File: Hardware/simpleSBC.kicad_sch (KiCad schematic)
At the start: 124 parts, among them J1 Conn_02x07_Odd_Even, J2 Micro_SD_Card_Det, J3 Conn_01x06_Male, U1 STM32MP157FAD1, U2 LP2998, U3 MT41K256M16TW, X1 ASCO, Y1 32.786

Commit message: Add STPMIC1
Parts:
- added C67, C68, C69, C70: 10u, Capacitor_SMD:C_0402_1005Metric, symbol Device:C_Small
- added C71, C72, C73, C74, C75: 1u, Capacitor_SMD:C_0402_1005Metric, symbol Device:C_Small
- added C76: 4.7u, Capacitor_SMD:C_0402_1005Metric, symbol Device:C_Small
- added L1, L2, L3, L4: L_Small, symbol Device:L_Small
- added R9: R_Small, symbol Device:R_Small
- added TP10: TestPoint, symbol Connector:TestPoint
- added U4: STPMIC1, BioMEMS:WFQFN44L, symbol BioMEMS:STPMIC1APQR
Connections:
- net +1V2: now also L1.2, U4.5 (VOUT1)
- net +1V35: now also L2.2, U4.13 (LDO3IN), U4.9 (VOUT2)
- net +3V3: now also L4.2, U4.31 (VOUT3), U4.42 (VIO)
- net GND: now also C67.1, C68.1, C69.1, C70.1, C71.2, C72.2, C73.2, C74.1, C75.1, C76.1, U4.10 (PGND2), U4.15 (GNDLDO), U4.26 (PGND4), U4.30 (PGND3), U4.32 (PGND5), U4.41 (AGND), U4.45 (EPGND), U4.6 (PGND1)
- net NRST: now also U4.1 (RSTn)
- net PWR_ON: now also U4.44 (PWRCTRL)
- net VREF_DDR: now also C74.2, U4.16 (VREFDDR)
- net VTT_DDR: now also C75.2, U4.14 (LDO3OUT)
- net PA0_WAKEUP: now reaches U1.N3 (PA0)
- net PA0_WAKEUP: now also U4.43 (INTn)
- new net: L1.1, U4.7 (VLX1)
- new net: R9.2, U4.37 (SWIN)
- new net: L2.1, U4.11 (VLX2)
- new net: TP10.1, U4.17 (PONKEYn)
- new net: L3.1, U4.25 (VLX4)
- new net: L4.1, U4.29 (VLX3)
- new net: C76.2, U4.40 (INTLDO)
- new net +3.3VP: C72.1, L3.2, U4.22 (LDO16IN), U4.27 (VOUT4)
- new net +5V: C67.2, C68.2, C69.2, C70.2, C71.1, C73.1, R9.1, U4.12 (BUCK2IN), U4.19 (LDO25IN), U4.24 (BUCK4IN), U4.28 (BUCK3IN), U4.33 (VLXBST), U4.36 (VIN), U4.8 (BUCK1IN)
- new net I2C4_SCL: U4.4 (SCL)
- new net I2C4_SDA: U4.3 (SDA)
- new net PMIC_WAKEUP: U4.2 (WAKEUP)
- no-connect marks 101 -> 108
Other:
- moved on the sheet: C1, C10, C11, C12, C13, C14, C15, C16, C17, C18, C19, C2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

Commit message: Remove old files
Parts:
- removed C1, C11, C13, C15, C18, C21, C23, C24, C26, C28, C3, C30, C31, C32, C35, C38, C42, C45, C48, C5, C7, C71, C72, C73, C74, C75: 1u, Capacitor_SMD:C_0402_1005Metric, symbol Device:C_Small
- removed C10, C17: 1n, Capacitor_SMD:C_0402_1005Metric, symbol Device:C_Small
- removed C12, C14, C16, C19, C2, C20, C22, C25, C27, C4, C46, C47, C49, C50, C52, C53, C54, C55, C56, C57, C58, C59, C6, C60, C61, C62, C63, C64, C8, C9: 100n, Capacitor_SMD:C_0402_1005Metric, symbol Device:C_Small
- removed C33, C34: 10u, Capacitor_SMD:C_0805_2012Metric, symbol Device:C_Small
- removed C39, C43, C44: 100u, Capacitor_SMD:C_1206_3216Metric, symbol Device:C_Polarized_Small_US
- removed C41, C76: 4.7u, Capacitor_SMD:C_0402_1005Metric, symbol Device:C_Small
- removed C51: 4.7u, Capacitor_SMD:C_0603_1608Metric, symbol Device:C_Small
- removed C65, C66: 22u, Capacitor_SMD:C_0805_2012Metric, symbol Device:C_Small
- removed C67, C68, C69, C70: 10u, Capacitor_SMD:C_0402_1005Metric, symbol Device:C_Small
- removed J2: Micro_SD_Card_Det, Connector_Card:microSD_HC_Molex_104031-0811, symbol Connector:Micro_SD_Card_Det
- removed JP1: SolderJumper_2_Bridged, Jumper:SolderJumper-2_P1.3mm_Bridged2Bar_Pad1.0x1.5mm, symbol Jumper:SolderJumper_2_Bridged
- removed L1, L2, L3, L4: L_Small, symbol Device:L_Small
- removed R1, R4: 240, Resistor_SMD:R_0402_1005Metric, symbol Device:R_Small
- removed R10, R11, R12, R13, R14: 47k, Resistor_SMD:R_0402_1005Metric, symbol Device:R_Small
- removed R15, R3, R5: 10k, Resistor_SMD:R_0402_1005Metric, symbol Device:R_Small
- removed R16, R17, R18, R19, R20, R21, R22, R23, R24, R25, R26, R27, R28, R29, R30, R31, R32, R33, R34, R35, R36, R37, R38, R39: 56, Resistor_SMD:R_0402_1005Metric, symbol Device:R_Small
- removed R2: 100, Resistor_SMD:R_0402_1005Metric, symbol Device:R_Small
- removed R9: R_Small, symbol Device:R_Small
- removed TP1, TP2, TP3, TP4, TP5, TP6: TestPoint-SP, personal:PROBE_PAD_1206, symbol Connector:TestPoint
- removed TP10: TestPoint, symbol Connector:TestPoint
- removed TP7, TP9: TestPoint, personal:PROBE_PAD_1206, symbol Connector:TestPoint
- removed unit 4 of U1
- removed unit 1 of U1
- removed U2: LP2998, Package_SO:SOIC-8-1EP_3.9x4.9mm_P1.27mm_EP2.29x3mm_ThermalVias, symbol Personal:LP2998
- removed U3: MT41K256M16TW, Package_BGA:BGA-96_9.0x13.0mm_Layout2x3x16_P0.8mm, symbol Personal:MT41K256M16TW
- removed U4: STPMIC1, BioMEMS:WFQFN44L, symbol BioMEMS:STPMIC1APQR
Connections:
- no-connect marks 108 -> 92
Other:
- added sheet Memory (memory.kicad_sch)
- added sheet Power (power.kicad_sch)
- note removed: "100nF"
- note removed: "Connect VDDQ near memory"
- note removed: "RAM"
- note removed: "SD Card"
- note removed: "Termination"
- note removed: "VDD"
- note removed: "VDDCORE"
- note removed: "VDD_DSI, VDD_PLL and VDD_ANA must be star-connected to VDD"
- moved on the sheet: C29, C36, C37, C40, D1, J1, J3, R40, R6, R7, R8, TP8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

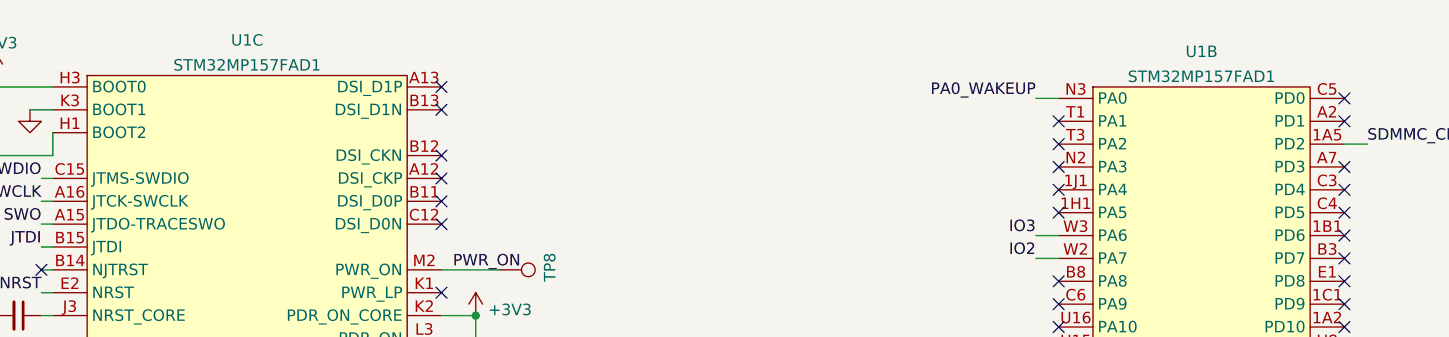
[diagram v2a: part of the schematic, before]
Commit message: Create libraries and move custom symbols to project specific libraries
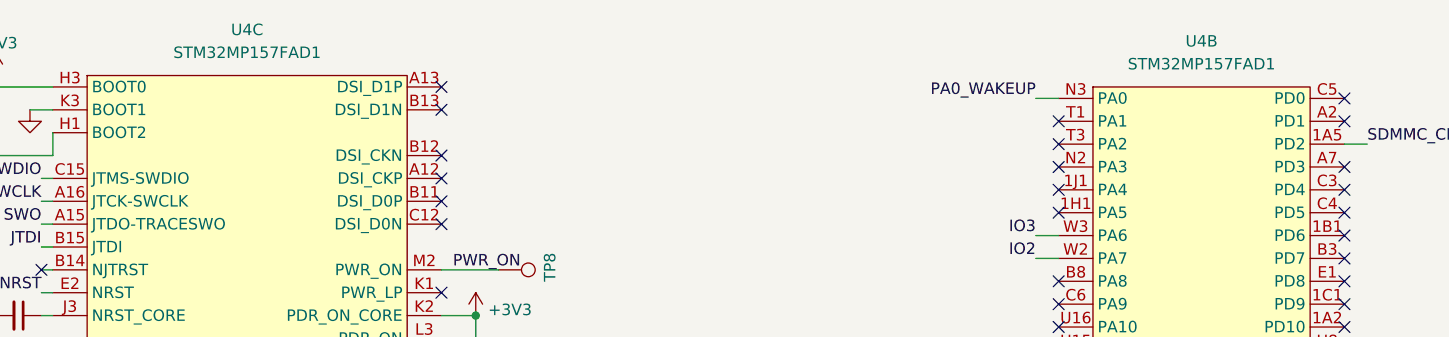
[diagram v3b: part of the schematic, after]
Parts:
- removed U1: STM32MP157FAD1, personal:TFBGA257, symbol Personal:STM32MP157FAD1
- added U4: STM32MP157FAD1, personal:TFBGA257, symbol SimpleSBC:STM32MP157FAD1
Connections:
- net +3V3: now also U4.H1 (BOOT2), U4.H3 (BOOT0), U4.K2 (PDR_ON_CORE), U4.L3 (PDR_ON)
- net GND: now also U4.A3 (PB7), U4.K3 (BOOT1)
- net IO1: now also U4.V1 (PC5)
- net IO2: now also U4.W2 (PA7)
- net IO3: now also U4.W3 (PA6)
- net IO4: now also U4.W4 (PF11)
- net IO5: now also U4.W7 (PF7)
- net IO6: now also U4.W8 (PG9)
- net JTDI: now also U4.B15 (JTDI)
- net NRST: now also U4.E2 (NRST)
- net PA0_WAKEUP: now also U4.N3 (PA0)
- net PWR_ON: now also U4.M2 (PWR_ON)
- net SDMMC_CLK: now also U4.1B4 (PC12)
- net SDMMC_CMD: now also U4.1A5 (PD2)
- net SDMMC_D0: now also U4.A9 (PC8)
- net SDMMC_D1: now also U4.B9 (PC9)
- net SDMMC_D2: now also U4.B10 (PC10)
- net SDMMC_D3: now also U4.C11 (PC11)
- net SWCLK: now also U4.A16 (JTCK-SWCLK)
- net SWDIO: now also U4.C15 (JTMS-SWDIO)
- net SWO: now also U4.A15 (JTDO-TRACESWO)
- net UART4_RX: now also U4.V13 (PB2)
- net UART4_TX: now also U4.U6 (PG11)
- net at C37.2, Y1.1: now also U4.F2 (PC15-OSC32_OUT)
- net at C36.2, Y1.2: now also U4.G2 (PC14-OSC32_IN)
- net at R40.2: now also U4.L2 (PA13)
- net at C40.1: now also U4.J3 (NRST_CORE)
- net at R8.2: now also U4.J2 (PH1-OSC_OUT)
- net at X1.3 (OUT): now also U4.H2 (PH0-OSC_IN)

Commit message: First Draft schematic (R2)
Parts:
- removed U4: STM32MP157FAD1, personal:TFBGA257, symbol SimpleSBC:STM32MP157FAD1
- added J5, J6: USB_A, Connector_USB:USB_A_Molex_67643_Horizontal, symbol Connector:USB_A
- added U1: STM32MP157FAD1, SimpleSBC:TFBGA257, symbol SimpleSBC:STM32MP157FAD1
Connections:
- net +3V3: now also U1.H1 (BOOT2), U1.H3 (BOOT0), U1.K2 (PDR_ON_CORE), U1.L3 (PDR_ON)
- net GND: now also J5.4 (GND), J5.5 (Shield), J6.4 (GND), J6.5 (Shield), U1.A3 (PB7), U1.K3 (BOOT1)
- net IO1: now also U1.V1 (PC5)
- net IO2: now also U1.W2 (PA7)
- net IO3: now also U1.W3 (PA6)
- net IO4: now also U1.W4 (PF11)
- net IO5: now also U1.W7 (PF7)
- net IO6: now also U1.W8 (PG9)
- net JTDI: now also U1.B15 (JTDI)
- net NRST: now also U1.E2 (NRST)
- net PA0_WAKEUP: now also U1.N3 (PA0)
- net PWR_ON: now also U1.M2 (PWR_ON)
- net SDMMC_CLK: now also U1.1B4 (PC12)
- net SDMMC_CMD: now also U1.1A5 (PD2)
- net SDMMC_D0: now also U1.A9 (PC8)
- net SDMMC_D1: now also U1.B9 (PC9)
- net SDMMC_D2: now also U1.B10 (PC10)
- net SDMMC_D3: now also U1.C11 (PC11)
- net SWCLK: now also U1.A16 (JTCK-SWCLK)
- net SWDIO: now also U1.C15 (JTMS-SWDIO)
- net SWO: now also U1.A15 (JTDO-TRACESWO)
- net UART4_RX: now also U1.V13 (PB2)
- net UART4_TX: now also U1.U6 (PG11)
- net at C37.2, Y1.1: now also U1.F2 (PC15-OSC32_OUT)
- net at C36.2, Y1.2: now also U1.G2 (PC14-OSC32_IN)
- net at R40.2: now also U1.L2 (PA13)
- net at X1.3 (OUT): now also U1.H2 (PH0-OSC_IN)
- net at R8.2: now also U1.J2 (PH1-OSC_OUT)
- net at C40.1: now also U1.J3 (NRST_CORE)
- new net: J5.2 (D-), U1.W10 (USB_DM2)
- new net: J5.3 (D+), U1.V10 (USB_DP2)
- new net: J6.2 (D-), U1.V14 (USB_DP1)
- new net: J6.3 (D+), U1.W14 (USB_DM1)
- no-connect marks 92 -> 90
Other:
- note added: "TODO: - I2C for STPMIC should be broken out - Add USB and Ethernet - USB Power?"
- title: Application Processor Test -> SimpleSBC
- moved on the sheet: J3

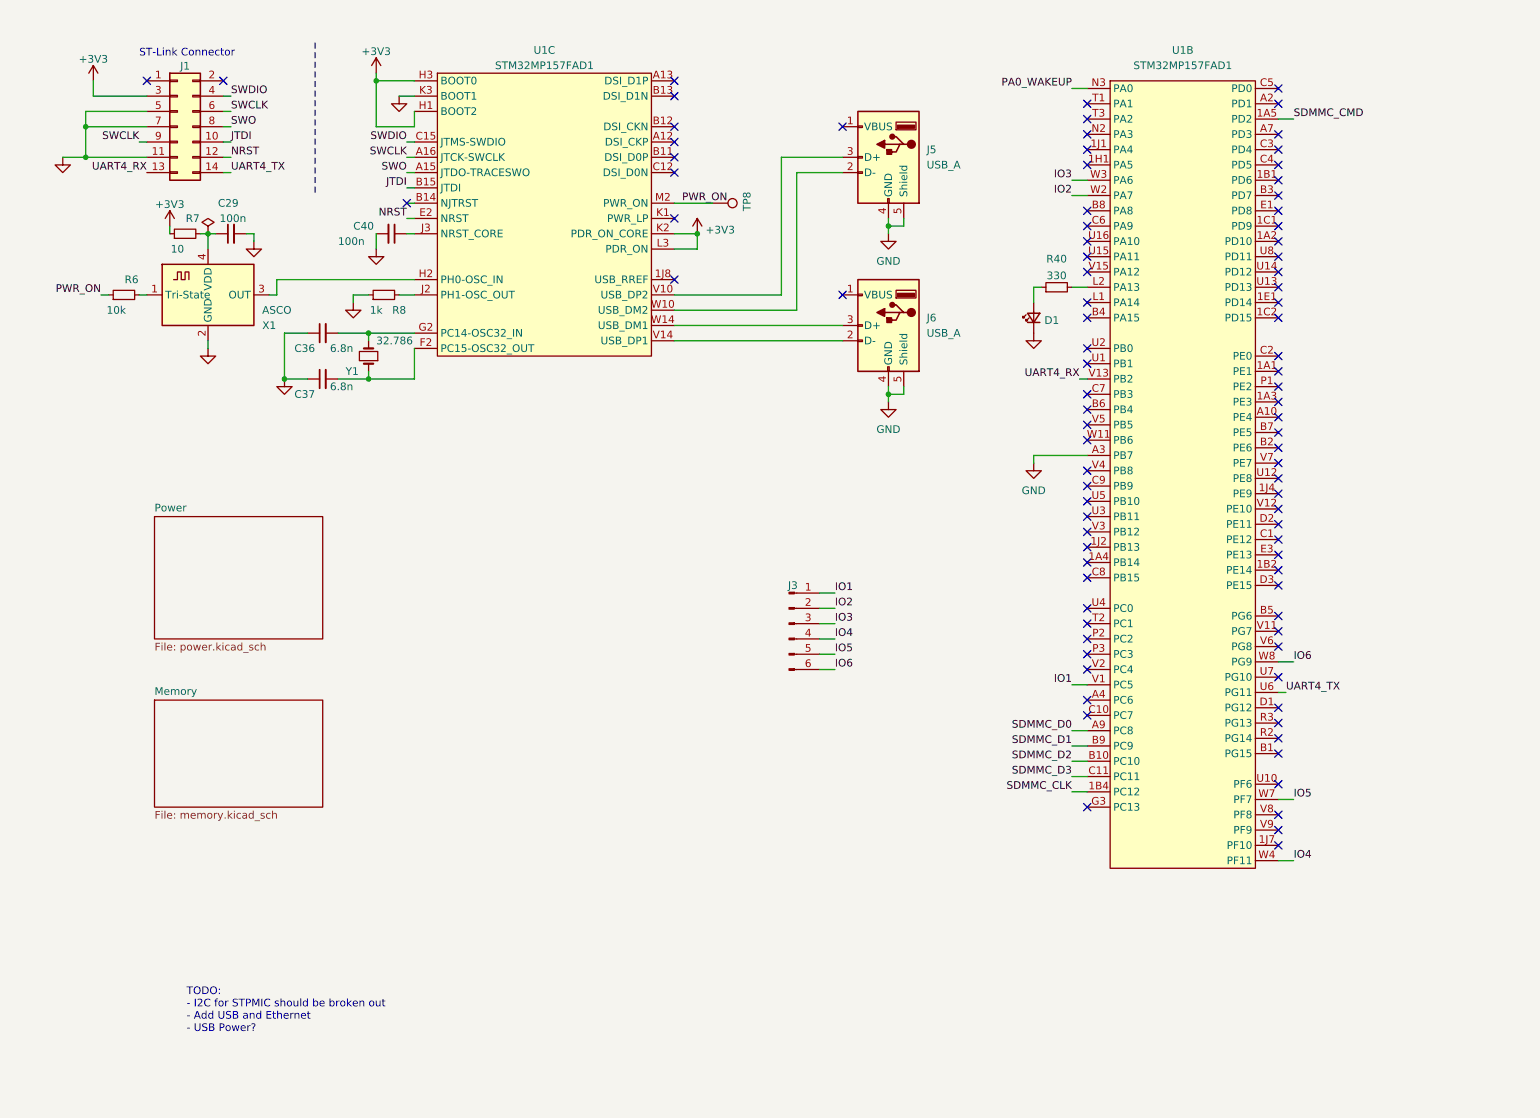
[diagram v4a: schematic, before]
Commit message: Add Ethernet and USB power switching
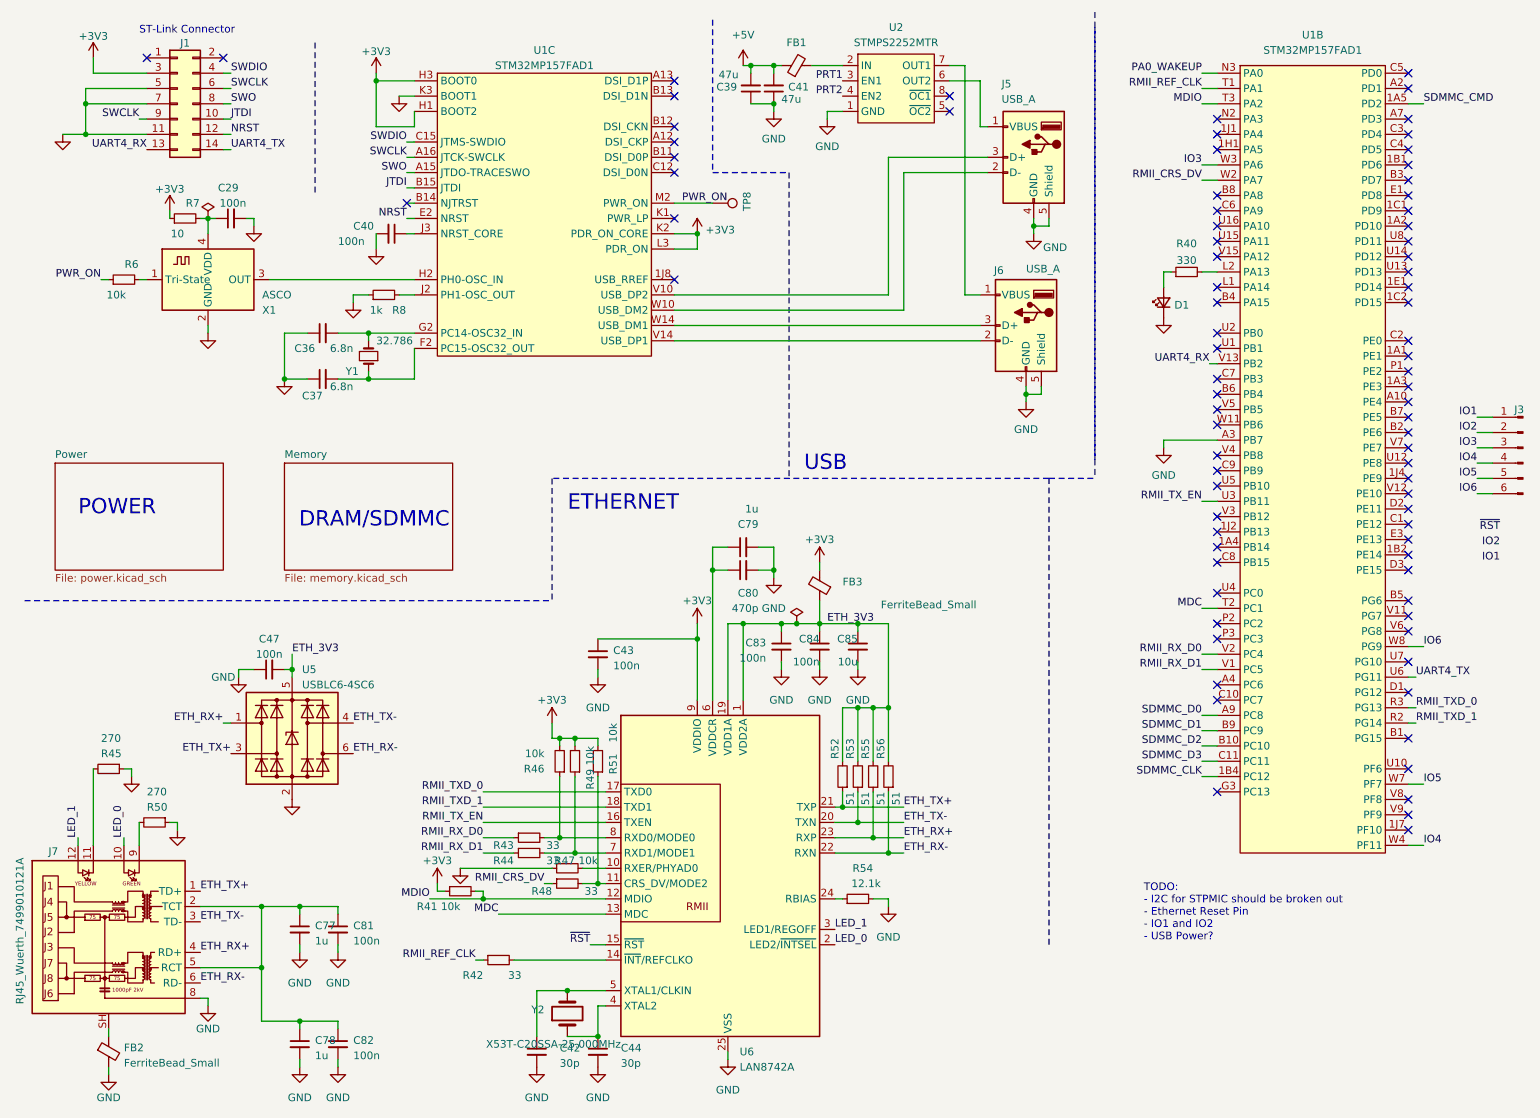
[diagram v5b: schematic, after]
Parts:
- added C39, C41: 47u, Capacitor_SMD:C_0402_1005Metric, symbol Device:C_Small
- added C42, C44: 30p, Capacitor_SMD:C_0603_1608Metric, symbol Device:C_Small
- added C43, C47, C81, C82, C83, C84: 100n, Capacitor_SMD:C_0603_1608Metric, symbol Device:C_Small
- added C77, C78, C79: 1u, Capacitor_SMD:C_0603_1608Metric, symbol Device:C_Small
- added C80: 470p, Capacitor_SMD:C_0603_1608Metric, symbol Device:C_Small
- added C85: 10u, Capacitor_SMD:C_0805_2012Metric, symbol Device:C_Small
- added FB1: FerriteBead_Small, symbol Device:FerriteBead_Small
- added FB2, FB3: FerriteBead_Small, Inductor_SMD:L_0603_1608Metric, symbol Device:FerriteBead_Small
- added J7: RJ45_Wuerth_7499010121A, Connector_RJ:RJ45_Wuerth_7499010121A_Horizontal, symbol SimpleSBC:RJ45_Wuerth_7499010121A
- added R41, R46, R47, R49, R51: 10k, Resistor_SMD:R_0603_1608Metric, symbol Device:R_Small
- added R42, R43, R44, R48: 33, Resistor_SMD:R_0603_1608Metric, symbol Device:R_Small
- added R45, R50: 270, Resistor_SMD:R_0603_1608Metric, symbol Device:R_Small
- added R52, R53, R55, R56: 51, Resistor_SMD:R_0603_1608Metric, symbol Device:R_Small
- added R54: 12.1k, Resistor_SMD:R_0603_1608Metric, symbol Device:R_Small
- added U2: STMPS2252MTR, Package_SO:SOIC-8_3.9x4.9mm_P1.27mm, symbol SimpleSBC:STMPS2252MTR
- added U5: USBLC6-4SC6, Package_TO_SOT_SMD:SOT-23-6, symbol Power_Protection:USBLC6-4SC6
- added U6: LAN8742A, Package_DFN_QFN:VQFN-24-1EP_4x4mm_P0.5mm_EP2.5x2.5mm_ThermalVias, symbol Interface_Ethernet:LAN8742A
- added Y2: X53T-C20SSA-25.000MHz, Crystal:Crystal_SMD_MicroCrystal_CM9V-T1A-2Pin_1.6x1.0mm, symbol Device:Crystal
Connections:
- net +3V3: now also C43.1, FB3.2, R41.1, R46.2, R49.2, R51.2, U6.9 (VDDIO)
- net GND: now also C39.1, C41.1, C42.2, C43.2, C44.2, C47.1, C77.2, C78.2, C79.2, C80.2, C81.2, C82.2, C83.2, C84.2, C85.2, FB2.2, J7.8, R45.1, R47.1, R50.1, R54.2, U2.1 (GND), U5.2 (GND), U6.25 (VSS)
- net IO1: no longer U1.V1 (PC5)
- net IO2: no longer U1.W2 (PA7)
- net at J5.1 (VBUS): now also U2.6 (OUT2)
- net at J6.1 (VBUS): now also U2.7 (OUT1)
- net RMII_TXD_1: now reaches U1.R2 (PG14)
- net RMII_TXD_1: now also U6.18 (TXD1)
- net RMII_TXD_0: now reaches U1.R3 (PG13)
- net RMII_TXD_0: now also U6.17 (TXD0)
- net RMII_REF_CLK: now reaches U1.T1 (PA1)
- net RMII_REF_CLK: now also R42.1
- net MDC: now reaches U1.T2 (PC1)
- net MDC: now also U6.13 (MDC)
- net MDIO: now reaches U1.T3 (PA2)
- net MDIO: now also R41.2, U6.12 (MDIO)
- net RMII_TX_EN: now reaches U1.U3 (PB11)
- net RMII_TX_EN: now also U6.16 (TXEN)
- net RMII_RX_D0: now reaches U1.V2 (PC4)
- net RMII_RX_D0: now also R43.1
- new net: R48.2, R51.1, U6.11 (CRS_DV/MODE2)
- new net: C77.1, C78.1, C81.1, C82.1, J7.2 (TCT), J7.5 (RCT)
- new net: C79.1, C80.1, U6.6 (VDDCR)
- new net: J7.9, R50.2
- new net: R44.2, R49.1, U6.7 (RXD1/MODE1)
- new net: J7.11, R45.2
- new net: FB2.1, J7.SH
- new net: R47.2, U6.10 (RXER/PHYAD0)
- new net: R42.2, U6.14 (~{INT}/REFCLKO)
- new net: R54.1, U6.24 (RBIAS)
- new net: C44.1, U6.4 (XTAL2), Y2.1
- new net: C42.1, U6.5 (XTAL1/CLKIN), Y2.2
- new net: R43.2, R46.1, U6.8 (RXD0/MODE0)
- new net: FB1.2, U2.2 (IN)
- new net +5V: C39.2, C41.2, FB1.1
- new net ETH_3V3: C47.2, C83.1, C84.1, C85.1, FB3.1, R52.2, R53.2, R55.2, R56.2, U5.5 (VBUS), U6.1 (VDD2A), U6.19 (VDD1A)
- new net ETH_RX+: J7.4 (RD+), R55.1, U5.1 (I/O1), U6.23 (RXP)
- new net ETH_RX-: J7.6 (RD-), R56.1, U5.6 (I/O4), U6.22 (RXN)
- new net ETH_TX+: J7.1 (TD+), R52.1, U5.3 (I/O2), U6.21 (TXP)
- new net ETH_TX-: J7.3 (TD-), R53.1, U5.4 (I/O3), U6.20 (TXN)
- new net LED_0: J7.10, U6.2 (LED2/~{INTSEL})
- new net LED_1: J7.12, U6.3 (LED1/REGOFF)
- new net PRT1: U2.3 (EN1)
- new net PRT2: U2.4 (EN2)
- new net RMII_CRS_DV: R48.1, U1.W2 (PA7)
- new net RMII_RX_D1: R44.1, U1.V1 (PC5)
- new net ~{RST}: U6.15 (~{RST})
- no-connect marks 90 -> 83
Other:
- note added: "DRAM/SDMMC"
- note added: "ETHERNET"
- note added: "POWER"
- note added: "TODO: - I2C for STPMIC should be broken out - Ethernet Reset Pin - IO1 and IO2 - USB Power?"
- note added: "USB"
- note removed: "TODO: - I2C for STPMIC should be broken out - Add USB and Ethernet - USB Power?"
- moved on the sheet: C29, D1, J1, J3, J5, J6, R40, R6, R7, U1B, X1
